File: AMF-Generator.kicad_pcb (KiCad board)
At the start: 4 copper layers, 71.5 x 76.5 mm, 71 parts, among them J1 SW_OUT, J2 CUR_SENSE, J3 PWR_IN, J4 I2C_5V, J5 I2C_3V3, Q1 ISC012N04LM6ATMA1, Q2 ISC012N04LM6ATMA1, U1 ACS732KLATR-75AB, U2 UCC21540, U3 LTC1968, U4 LT1880, U5 CAT3200-5, U6 NLSX4373DR2G, U7 ADC101C027CIMK, U8 74LVC1G06, U9 QTPY

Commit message: Added bypass cap to inverter and some cleanup
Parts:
- added C5: 0.1uF, Capacitor_SMD:C_0805_2012Metric, F.Cu at (117.8, 62.2)
- moved D1 4.91 mm to (127.1, 47.5)
- moved C1 4.91 mm to (137.2, 49.2)
- moved C2 4.91 mm to (141.8, 68.2)
- moved C22 4.91 mm to (139.0, 71.8)
- moved C23 4.91 mm to (126.8, 79.8)
- moved C24 4.91 mm to (128.2, 86.3)
- moved C26 4.91 mm to (122.2, 88.2)
- moved C27 4.91 mm to (112.2, 70.5)
- moved C29 4.91 mm to (109.8, 80.0)
- moved C3 4.91 mm to (139.2, 49.2)
- moved C30 4.91 mm to (115.5, 88.0)
- moved C31 4.91 mm to (120.8, 79.8)
- moved C32 4.91 mm to (112.2, 83.6)
- moved C33 4.91 mm to (111.0, 90.0)
- moved C34 4.91 mm to (137.1, 68.5)
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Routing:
- net +5V: track 20.5 -> 23.0 mm
- net GND: track 32.8 -> 33.8 mm, vias 65 -> 66
- net PWM_B: track 26.0 -> 25.4 mm
- net AC_A: vias 64 -> 66

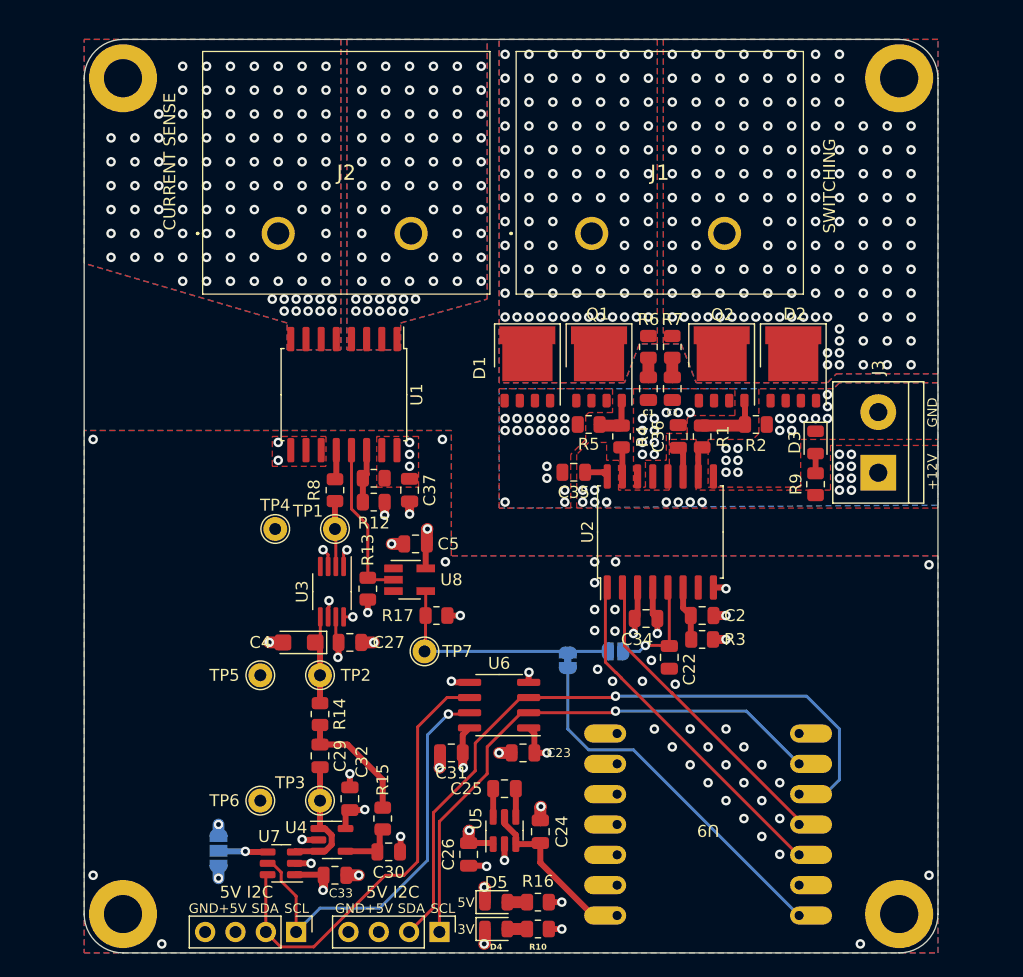
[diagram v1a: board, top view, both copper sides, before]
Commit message: Update to improved barrier block and cap bank pcb nearly done
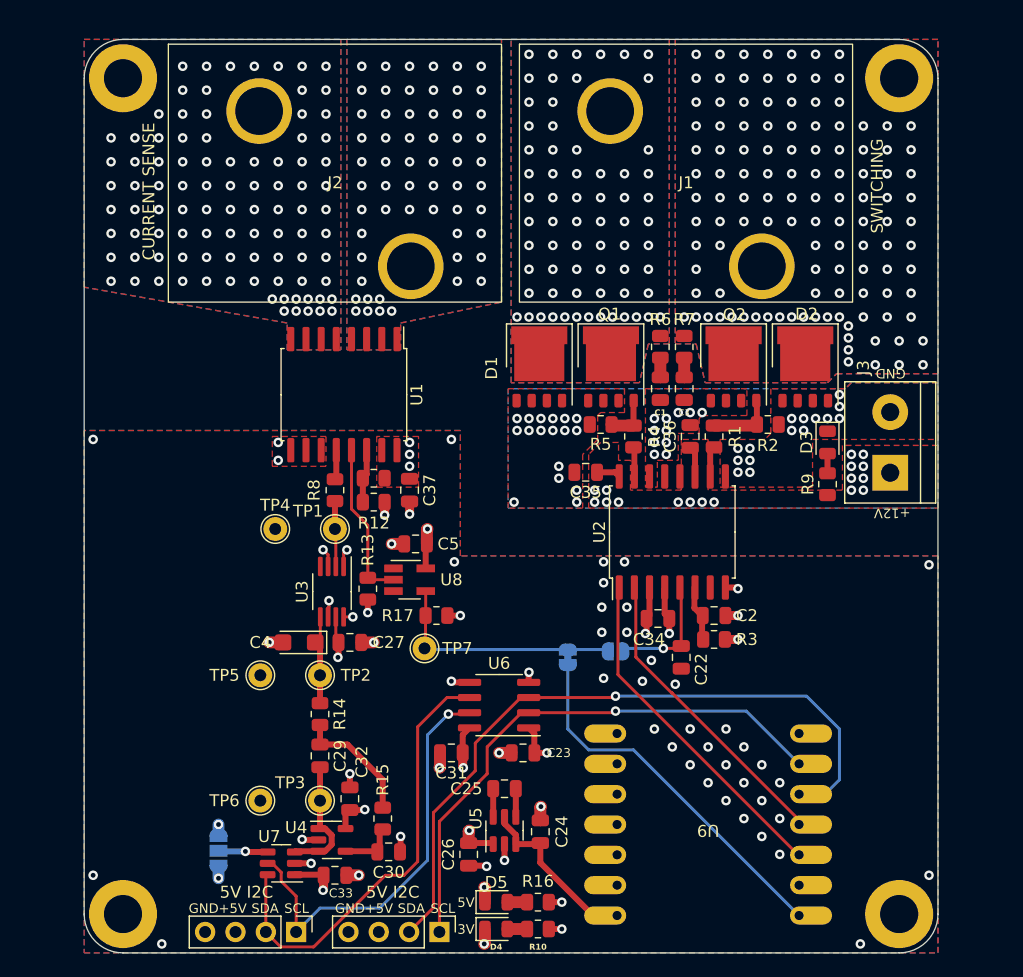
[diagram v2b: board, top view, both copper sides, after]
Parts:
- J1, J2: footprint 8PCV-02-006:8PCV02006 -> BarrierBlock:0389690002
- R1, R4: value 20 -> 4.7
- moved J1 8.74 mm to (140.4, 32.5), turned to 0 degrees
- moved J2 6.05 mm to (111.0, 32.5), turned to 0 degrees
- moved D1 1.00 mm to (128.1, 47.5)
- moved C1 1.00 mm to (138.2, 49.2)
- moved C2 1.00 mm to (142.8, 68.2)
- moved C22 1.00 mm to (140.0, 71.8)
- moved C3 1.00 mm to (140.2, 49.2)
- moved C34 1.00 mm to (138.1, 68.5)
- moved C35 1.00 mm to (132.0, 56.2)
- moved C36 1.00 mm to (140.8, 53.2)
- moved D2 1.00 mm to (150.4, 47.5)
- moved D3 1.00 mm to (152.2, 53.8)
- moved J3 1.00 mm to (157.5, 56.3)
- moved Q1 1.00 mm to (134.1, 47.5)
- moved Q2 1.00 mm to (144.4, 47.5)
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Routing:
- net Net-(JP1-B): track 8.68 -> 9.54 mm
- net SW_B: vias 137 -> 118
- net SW_A: vias 86 -> 67
- net GND: vias 66 -> 65
- net AC_B: vias 95 -> 94
- net AC_A: vias 66 -> 58

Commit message: cleanup
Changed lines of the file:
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@@
   (segment (start 138.5 71) (end 139.8 71) (width 0.25) (layer "F.Cu") (net 48))
   (via (at 138.5 71) (size 0.8) (drill 0.4) (layers "F.Cu" "B.Cu") (net 48))
-  (segment (start 135.4 71) (end 135.15 71.25) (width 0.25) (layer "B.Cu") (net 48))
   (segment (start 138.5 71) (end 135.4 71) (width 0.25) (layer "B.Cu") (net 48))
   (segment (start 130.5 77.75) (end 132.25 79.5) (width 0.25) (layer "B.Cu") (net 49))

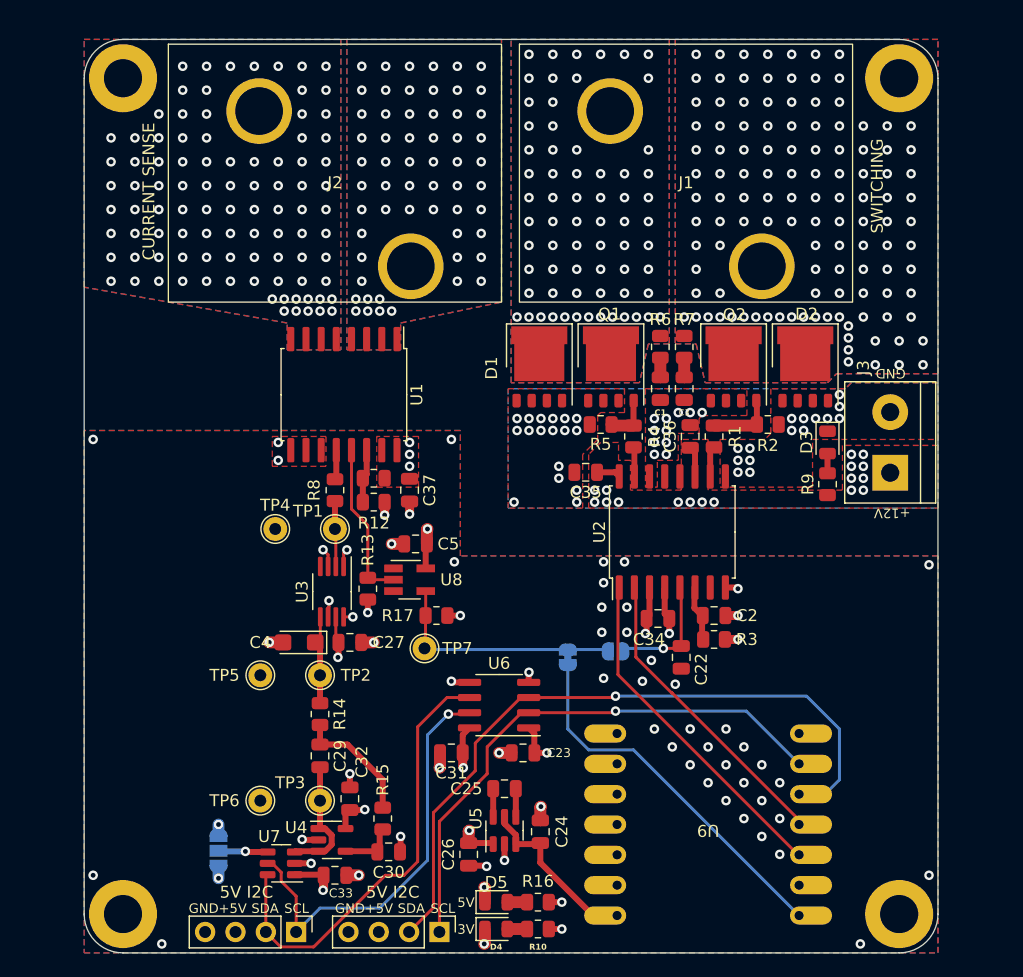
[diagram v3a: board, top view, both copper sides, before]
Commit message: made dimensions multiples of 10 mm
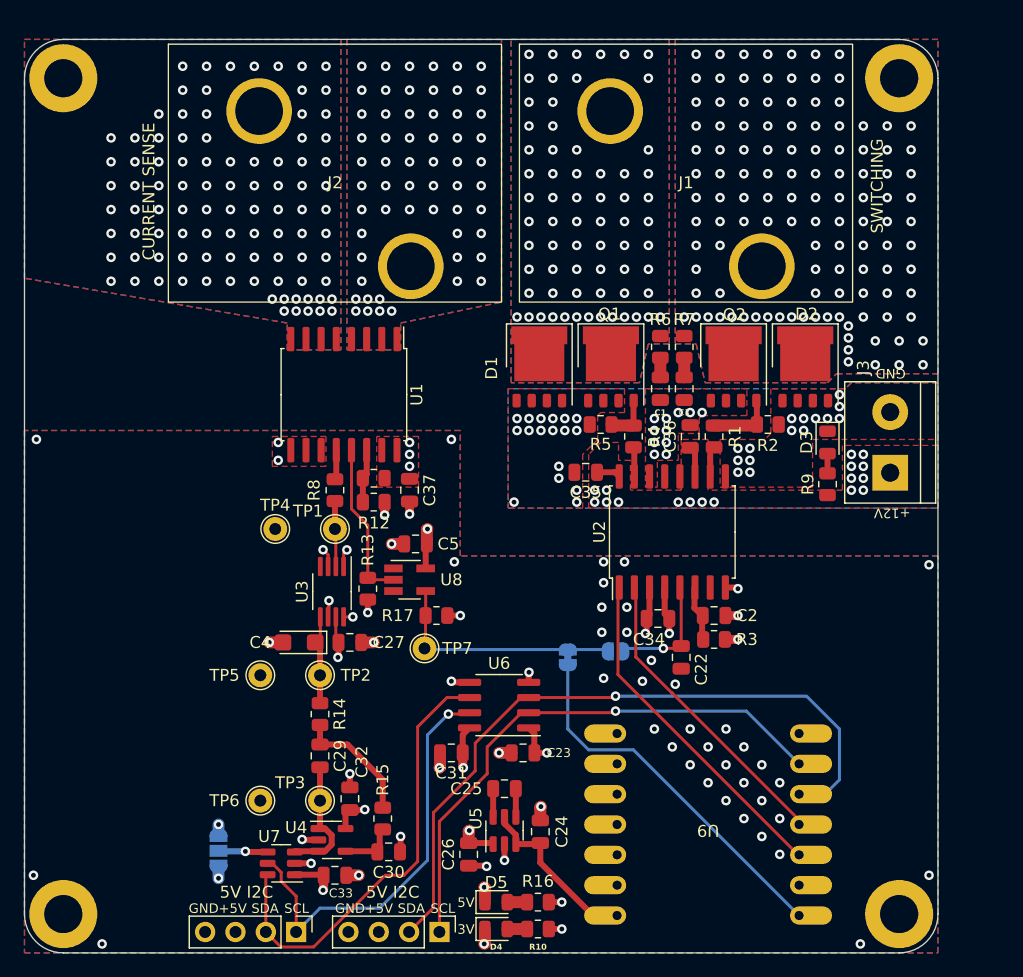
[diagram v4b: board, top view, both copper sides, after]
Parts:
- moved H1 5.00 mm to (88.2, 23.2)
- moved H3 5.00 mm to (88.2, 93.2)
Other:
- board size 71.5 x 76.5 mm -> 76.5 x 76.5 mm
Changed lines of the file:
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@@
   )
   (footprint "MountingHole:MountingHole_3.2mm_M3_ISO7380_Pad" (layer "F.Cu")
-    (at 93.25 93.25)
+    (at 88.25 93.25)
     (descr "Mounting Hole 3.2mm, M3, ISO7380")
     (tags "mounting hole 3.2mm m3 iso7380")
@@
   )
   (footprint "MountingHole:MountingHole_3.2mm_M3_ISO7380_Pad" (layer "F.Cu")
-    (at 93.25 23.25)
+    (at 88.25 23.25)
     (descr "Mounting Hole 3.2mm, M3, ISO7380")
     (tags "mounting hole 3.2mm m3 iso7380")
@@
       ))
   )
-  (gr_arc (start 93.25 96.5) (mid 90.951903 95.548097) (end 90 93.25)
+  (gr_arc (start 88.25 96.5) (mid 85.951903 95.548097) (end 85 93.25)
     (stroke (width 0.1) (type default)) (layer "Edge.Cuts"))
-  (gr_arc (start 90 23.25) (mid 90.951903 20.951903) (end 93.25 20)
+  (gr_arc (start 85 23.25) (mid 85.951903 20.951903) (end 88.25 20)
     (stroke (width 0.1) (type default)) (layer "Edge.Cuts"))
   (gr_arc (start 158.25 20) (mid 160.548097 20.951903) (end 161.5 23.25)
@@
   (gr_arc (start 161.5 93.25) (mid 160.548097 95.548097) (end 158.25 96.5)
     (stroke (width 0.1) (type default)) (layer "Edge.Cuts"))
-  (gr_line (start 158.25 96.5) (end 93.25 96.5)
+  (gr_line (start 158.25 96.5) (end 88.25 96.5)
     (stroke (width 0.1) (type default)) (layer "Edge.Cuts"))
-  (gr_line (start 90 93.25) (end 90 23.25)
+  (gr_line (start 85 93.25) (end 85 23.25)
     (stroke (width 0.1) (type default)) (layer "Edge.Cuts"))
   (gr_line (start 161.5 23.25) (end 161.5 93.25)
     (stroke (width 0.1) (type default)) (layer "Edge.Cuts"))
-  (gr_line (start 93.25 20) (end 158.25 20)
+  (gr_line (start 88.25 20) (end 158.25 20)
     (stroke (width 0.1) (type default)) (layer "Edge.Cuts"))
   (gr_text "+12V" (at 160.5 57.75 -90) (layer "B.SilkS")
@@
   (via (at 108.25 87) (size 0.8) (drill 0.4) (layers "F.Cu" "B.Cu") (net 4))
   (via (at 106.25 53.75) (size 0.8) (drill 0.4) (layers "F.Cu" "B.Cu") (free) (net 4))
-  (via (at 90.75 53.5) (size 0.8) (drill 0.4) (layers "F.Cu" "B.Cu") (free) (net 4))
+  (via (at 86 53.5) (size 0.8) (drill 0.4) (layers "F.Cu" "B.Cu") (free) (net 4))
   (via (at 128.25 84.25) (size 0.8) (drill 0.4) (layers "F.Cu" "B.Cu") (net 4))
   (via (at 120.75 53.5) (size 0.8) (drill 0.4) (layers "F.Cu" "B.Cu") (free) (net 4))
@@
   (via (at 110.5 67) (size 0.8) (drill 0.4) (layers "F.Cu" "B.Cu") (net 4))
   (via (at 160.75 90) (size 0.8) (drill 0.4) (layers "F.Cu" "B.Cu") (free) (net 4))
-  (via (at 96.5 95.75) (size 0.8) (drill 0.4) (layers "F.Cu" "B.Cu") (free) (net 4))
+  (via (at 91.5 95.75) (size 0.8) (drill 0.4) (layers "F.Cu" "B.Cu") (free) (net 4))
   (via (at 123.5 95.75) (size 0.8) (drill 0.4) (layers "F.Cu" "B.Cu") (net 4))
   (via (at 143.75 77.75) (size 0.8) (drill 0.4) (layers "F.Cu" "B.Cu") (free) (net 4))
@@
   (via (at 139.25 79.25) (size 0.8) (drill 0.4) (layers "F.Cu" "B.Cu") (free) (net 4))
   (via (at 160.75 64) (size 0.8) (drill 0.4) (layers "F.Cu" "B.Cu") (free) (net 4))
-  (via (at 90.75 90) (size 0.8) (drill 0.4) (layers "F.Cu" "B.Cu") (free) (net 4))
+  (via (at 85.75 90) (size 0.8) (drill 0.4) (layers "F.Cu" "B.Cu") (free) (net 4))
   (via (at 112 62.75) (size 0.8) (drill 0.4) (layers "F.Cu" "B.Cu") (net 4))
   (via (at 125.2 88.75) (size 0.8) (drill 0.4) (layers "F.Cu" "B.Cu") (net 4))
@@
         (xy 121.5 63.25)
         (xy 121.5 52.75)
-        (xy 90 52.75)
-        (xy 90 96.5)
+        (xy 85 52.75)
+        (xy 85 96.5)
         (xy 161.5 96.5)
         (xy 161.5 63.25)
@@
         (xy 107 46)
         (xy 107 43.75)
-        (xy 90 40.75)
-        (xy 90 20)
+        (xy 85 40)
+        (xy 85 20)
         (xy 111.5 20)
       )
@@
     (polygon
       (pts
-        (xy 90 52.75)
-        (xy 90 96.5)
+        (xy 85 52.75)
+        (xy 85 96.5)
         (xy 161.5 96.5)
         (xy 161.5 63.25)
@@
     (polygon
       (pts
-        (xy 90 52.75)
-        (xy 90 96.5)
+        (xy 85 52.75)
+        (xy 85 96.5)
         (xy 161.5 96.5)
         (xy 161.5 63.25)

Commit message: Layout updated. Silk still WIP
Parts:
- removed C23: 0.1uF, Capacitor_SMD:C_0805_2012Metric
- added R18: 5.6K, Resistor_SMD:R_0805_2012Metric, F.Cu at (130.0, 77.1)
- added R19: 5.6K, Resistor_SMD:R_0805_2012Metric, F.Cu at (130.0, 73.6)
- added R20: 5.6K, Resistor_SMD:R_0805_2012Metric, F.Cu at (120.8, 77.2)
- added R21: 5.6K, Resistor_SMD:R_0805_2012Metric, F.Cu at (120.8, 73.5)
- added R22: 200K, Resistor_SMD:R_0805_2012Metric_Pad1.20x1.40mm_HandSolder, F.Cu at (123.5, 80.8)
- U6: value NLSX4373DR2G -> LSF0102; footprint Package_SO:SOIC-8_3.9x4.9mm_P1.27mm -> Package_SO:SSOP-8_2.95x2.8mm_P0.65mm
- moved J5 42.4 mm to (159.5, 80.0), turned to 0 degrees
- moved C31 2.93 mm to (123.5, 78.8)
- moved U6 1.08 mm to (125.8, 76.0)
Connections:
- C31 pad 1: +5V -> Net-(U6-EN)
- U6 pad 1: +3V3 -> GND
- U6 pad 2: SCL_3V3 -> +3V3
- U6 pad 3: SDA_3V3 -> SCL_3V3
- U6 pad 4: GND -> SDA_3V3
- U6 pad 5: +3V3 -> SDA_5
- U6 pad 6: SDA_5 -> SCL_5
- U6 pad 7: SCL_5 -> Net-(U6-EN)
- U6 pad 8: +5V -> Net-(U6-EN)
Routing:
- net SDA_3V3: track 56.3 -> 43.3 mm
- net SCL_3V3: track 45.7 -> 34.5 mm
- net Net-(U6-EN): track 0.00 -> 4.59 mm
- net GND: track 33.8 -> 30.7 mm, vias 65 -> 63
- net SDA_5: track 37.5 -> 40.1 mm
- net SCL_5: track 34.7 -> 37.0 mm
- net +3V3: track 11.7 -> 12.3 mm
- net +5V: track 22.8 -> 22.5 mm, vias 12 -> 14
